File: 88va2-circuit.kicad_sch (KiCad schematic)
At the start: 0 parts

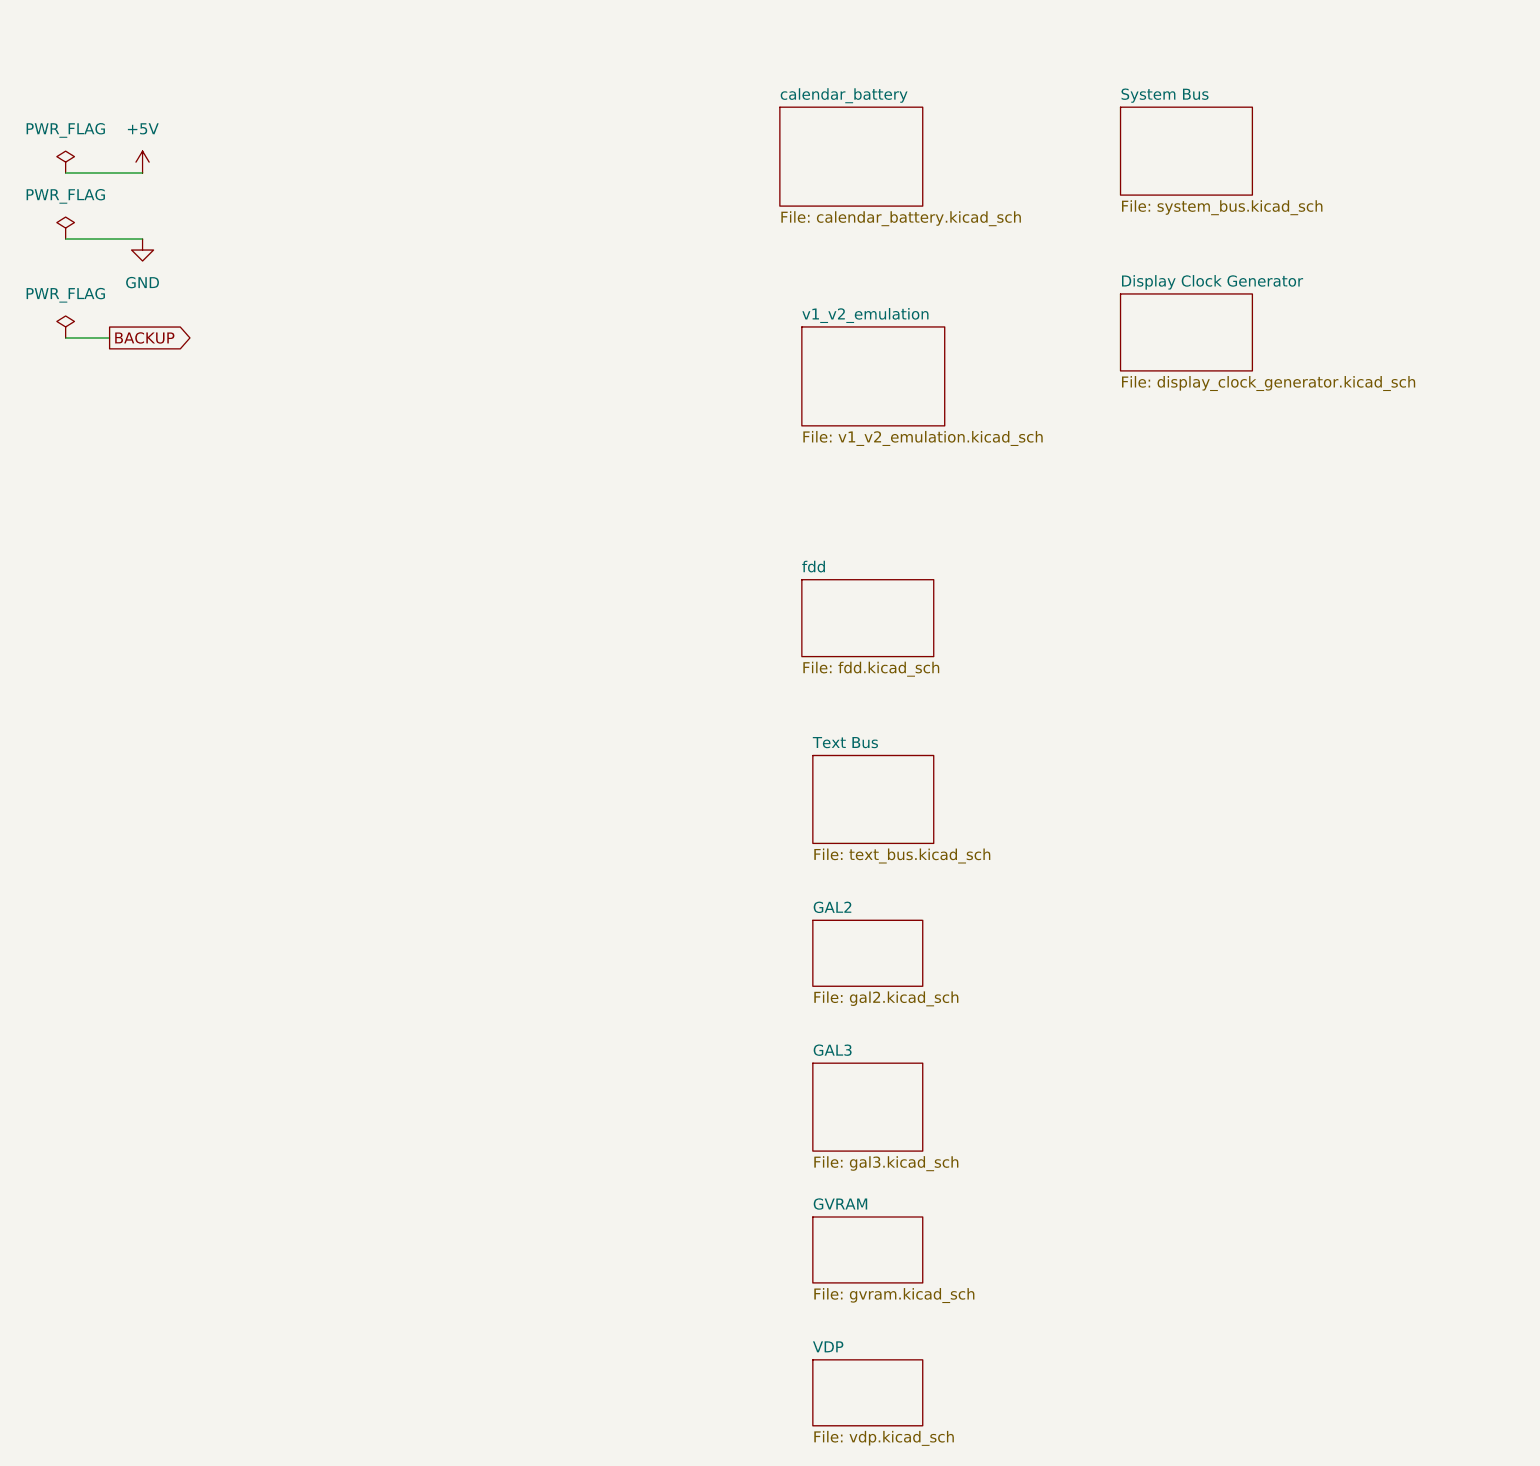
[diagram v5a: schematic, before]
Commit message: schematic: tidy hierarchical sheets
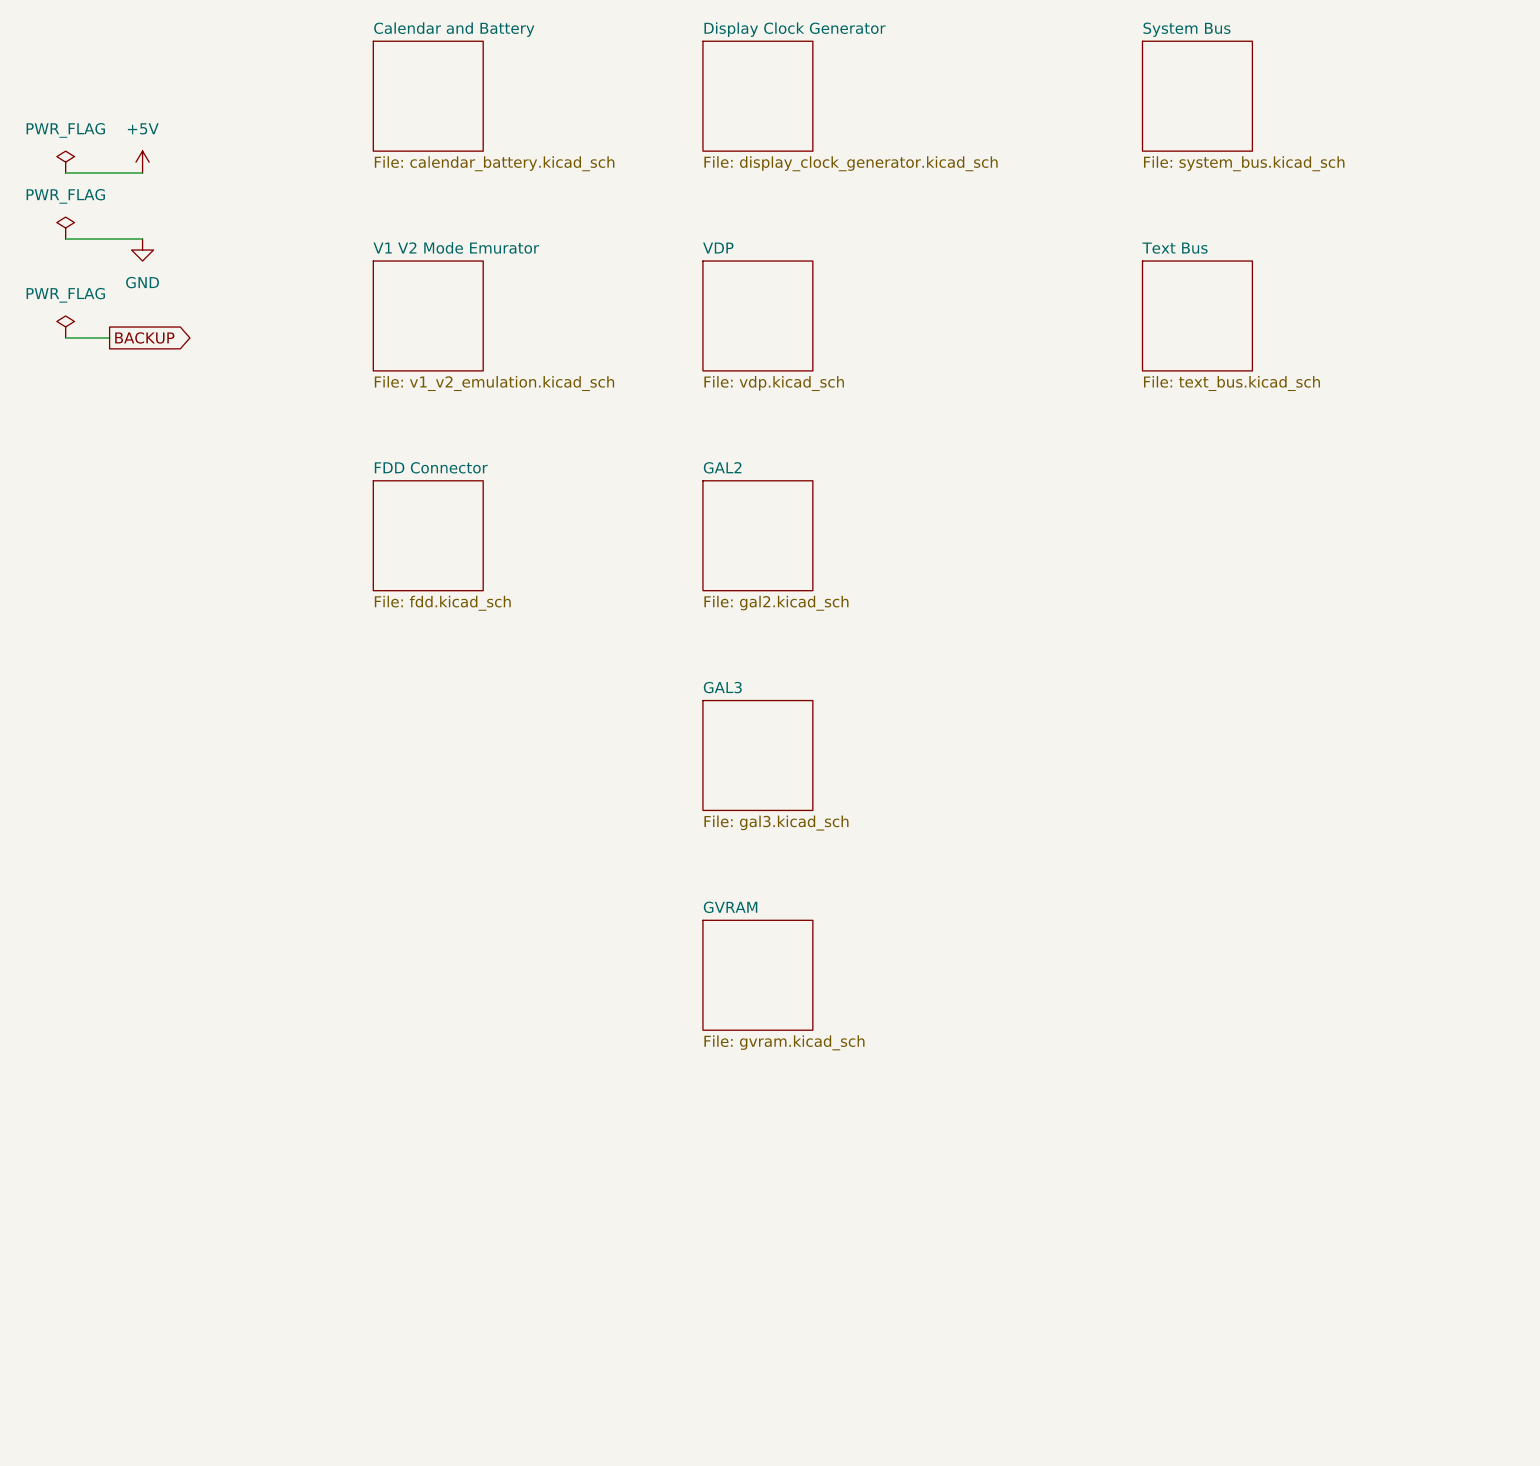
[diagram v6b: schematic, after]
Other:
- sheet calendar_battery renamed Calendar and Battery
- sheet fdd renamed FDD Connector
- sheet v1_v2_emulation renamed V1 V2 Mode Emurator
- title: (none) -> PC-88VA2 メイン基板 PWD-665
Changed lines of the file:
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@@
 (kicad_sch (version 20230121) (generator eeschema)
   (paper "A4")
+  (title_block
+    (title "PC-88VA2 メイン基板 PWD-665")
+  )
   (wire (pts (xy 40.64 59.69) (xy 45.72 59.69))
     (stroke (width 0) (type default))
@@
     )
   )
-  (sheet (at 125.73 87.63) (size 15.24 8.89) (fields_autoplaced)
-    (stroke (width 0.1524) (type solid))
-    (fill (color 0 0 0 0.0000))
-    (property "Sheetname" "fdd" (at 125.73 86.9184 0)
-      (effects (font (size 1.27 1.27)) (justify left bottom))
-    )
-    (property "Sheetfile" "fdd.kicad_sch" (at 125.73 97.1046 0)
+  (sheet (at 76.2 76.2) (size 12.7 12.7) (fields_autoplaced)
+    (stroke (width 0.1524) (type solid))
+    (fill (color 0 0 0 0.0000))
+    (property "Sheetname" "FDD Connector" (at 76.2 75.4884 0)
+      (effects (font (size 1.27 1.27)) (justify left bottom))
+    )
+    (property "Sheetfile" "fdd.kicad_sch" (at 76.2 89.4846 0)
       (effects (font (size 1.27 1.27)) (justify left top))
     )
@@
     )
   )
-  (sheet (at 125.73 58.42) (size 16.51 11.43) (fields_autoplaced)
-    (stroke (width 0.1524) (type solid))
-    (fill (color 0 0 0 0.0000))
-    (property "Sheetname" "v1_v2_emulation" (at 125.73 57.7084 0)
-      (effects (font (size 1.27 1.27)) (justify left bottom))
-    )
-    (property "Sheetfile" "v1_v2_emulation.kicad_sch" (at 125.73 70.4346 0)
+  (sheet (at 76.2 50.8) (size 12.7 12.7) (fields_autoplaced)
+    (stroke (width 0.1524) (type solid))
+    (fill (color 0 0 0 0.0000))
+    (property "Sheetname" "V1 V2 Mode Emurator" (at 76.2 50.0884 0)
+      (effects (font (size 1.27 1.27)) (justify left bottom))
+    )
+    (property "Sheetfile" "v1_v2_emulation.kicad_sch" (at 76.2 64.0846 0)
       (effects (font (size 1.27 1.27)) (justify left top))
     )
@@
     )
   )
-  (sheet (at 162.56 33.02) (size 15.24 10.16) (fields_autoplaced)
-    (stroke (width 0.1524) (type solid))
-    (fill (color 0 0 0 0.0000))
-    (property "Sheetname" "System Bus" (at 162.56 32.3084 0)
-      (effects (font (size 1.27 1.27)) (justify left bottom))
-    )
-    (property "Sheetfile" "system_bus.kicad_sch" (at 162.56 43.7646 0)
+  (sheet (at 165.1 25.4) (size 12.7 12.7) (fields_autoplaced)
+    (stroke (width 0.1524) (type solid))
+    (fill (color 0 0 0 0.0000))
+    (property "Sheetname" "System Bus" (at 165.1 24.6884 0)
+      (effects (font (size 1.27 1.27)) (justify left bottom))
+    )
+    (property "Sheetfile" "system_bus.kicad_sch" (at 165.1 38.6846 0)
       (effects (font (size 1.27 1.27)) (justify left top))
     )
@@
     )
   )
-  (sheet (at 127 143.51) (size 12.7 10.16) (fields_autoplaced)
-    (stroke (width 0.1524) (type solid))
-    (fill (color 0 0 0 0.0000))
-    (property "Sheetname" "GAL3" (at 127 142.7984 0)
-      (effects (font (size 1.27 1.27)) (justify left bottom))
-    )
-    (property "Sheetfile" "gal3.kicad_sch" (at 127 154.2546 0)
+  (sheet (at 114.3 101.6) (size 12.7 12.7) (fields_autoplaced)
+    (stroke (width 0.1524) (type solid))
+    (fill (color 0 0 0 0.0000))
+    (property "Sheetname" "GAL3" (at 114.3 100.8884 0)
+      (effects (font (size 1.27 1.27)) (justify left bottom))
+    )
+    (property "Sheetfile" "gal3.kicad_sch" (at 114.3 114.8846 0)
       (effects (font (size 1.27 1.27)) (justify left top))
     )
@@
     )
   )
-  (sheet (at 127 161.29) (size 12.7 7.62) (fields_autoplaced)
-    (stroke (width 0.1524) (type solid))
-    (fill (color 0 0 0 0.0000))
-    (property "Sheetname" "GVRAM" (at 127 160.5784 0)
-      (effects (font (size 1.27 1.27)) (justify left bottom))
-    )
-    (property "Sheetfile" "gvram.kicad_sch" (at 127 169.4946 0)
+  (sheet (at 114.3 127) (size 12.7 12.7) (fields_autoplaced)
+    (stroke (width 0.1524) (type solid))
+    (fill (color 0 0 0 0.0000))
+    (property "Sheetname" "GVRAM" (at 114.3 126.2884 0)
+      (effects (font (size 1.27 1.27)) (justify left bottom))
+    )
+    (property "Sheetfile" "gvram.kicad_sch" (at 114.3 140.2846 0)
       (effects (font (size 1.27 1.27)) (justify left top))
     )
@@
     )
   )
-  (sheet (at 127 107.95) (size 13.97 10.16) (fields_autoplaced)
-    (stroke (width 0.1524) (type solid))
-    (fill (color 0 0 0 0.0000))
-    (property "Sheetname" "Text Bus" (at 127 107.2384 0)
-      (effects (font (size 1.27 1.27)) (justify left bottom))
-    )
-    (property "Sheetfile" "text_bus.kicad_sch" (at 127 118.6946 0)
+  (sheet (at 165.1 50.8) (size 12.7 12.7) (fields_autoplaced)
+    (stroke (width 0.1524) (type solid))
+    (fill (color 0 0 0 0.0000))
+    (property "Sheetname" "Text Bus" (at 165.1 50.0884 0)
+      (effects (font (size 1.27 1.27)) (justify left bottom))
+    )
+    (property "Sheetfile" "text_bus.kicad_sch" (at 165.1 64.0846 0)
       (effects (font (size 1.27 1.27)) (justify left top))
     )
@@
     )
   )
-  (sheet (at 162.56 54.61) (size 15.24 8.89) (fields_autoplaced)
-    (stroke (width 0.1524) (type solid))
-    (fill (color 0 0 0 0.0000))
-    (property "Sheetname" "Display Clock Generator" (at 162.56 53.8984 0)
-      (effects (font (size 1.27 1.27)) (justify left bottom))
-    )
-    (property "Sheetfile" "display_clock_generator.kicad_sch" (at 162.56 64.0846 0)
+  (sheet (at 114.3 25.4) (size 12.7 12.7) (fields_autoplaced)
+    (stroke (width 0.1524) (type solid))
+    (fill (color 0 0 0 0.0000))
+    (property "Sheetname" "Display Clock Generator" (at 114.3 24.6884 0)
+      (effects (font (size 1.27 1.27)) (justify left bottom))
+    )
+    (property "Sheetfile" "display_clock_generator.kicad_sch" (at 114.3 38.6846 0)
       (effects (font (size 1.27 1.27)) (justify left top))
     )
@@
     )
   )
-  (sheet (at 127 177.8) (size 12.7 7.62) (fields_autoplaced)
-    (stroke (width 0.1524) (type solid))
-    (fill (color 0 0 0 0.0000))
-    (property "Sheetname" "VDP" (at 127 177.0884 0)
-      (effects (font (size 1.27 1.27)) (justify left bottom))
-    )
-    (property "Sheetfile" "vdp.kicad_sch" (at 127 186.0046 0)
+  (sheet (at 114.3 50.8) (size 12.7 12.7) (fields_autoplaced)
+    (stroke (width 0.1524) (type solid))
+    (fill (color 0 0 0 0.0000))
+    (property "Sheetname" "VDP" (at 114.3 50.0884 0)
+      (effects (font (size 1.27 1.27)) (justify left bottom))
+    )
+    (property "Sheetfile" "vdp.kicad_sch" (at 114.3 64.0846 0)
       (effects (font (size 1.27 1.27)) (justify left top))
     )
@@
     )
   )
-  (sheet (at 123.19 33.02) (size 16.51 11.43) (fields_autoplaced)
-    (stroke (width 0.1524) (type solid))
-    (fill (color 0 0 0 0.0000))
-    (property "Sheetname" "calendar_battery" (at 123.19 32.3084 0)
-      (effects (font (size 1.27 1.27)) (justify left bottom))
-    )
-    (property "Sheetfile" "calendar_battery.kicad_sch" (at 123.19 45.0346 0)
+  (sheet (at 76.2 25.4) (size 12.7 12.7) (fields_autoplaced)
+    (stroke (width 0.1524) (type solid))
+    (fill (color 0 0 0 0.0000))
+    (property "Sheetname" "Calendar and Battery" (at 76.2 24.6884 0)
+      (effects (font (size 1.27 1.27)) (justify left bottom))
+    )
+    (property "Sheetfile" "calendar_battery.kicad_sch" (at 76.2 38.6846 0)
       (effects (font (size 1.27 1.27)) (justify left top))
     )
@@
     )
   )
-  (sheet (at 127 127) (size 12.7 7.62) (fields_autoplaced)
-    (stroke (width 0.1524) (type solid))
-    (fill (color 0 0 0 0.0000))
-    (property "Sheetname" "GAL2" (at 127 126.2884 0)
-      (effects (font (size 1.27 1.27)) (justify left bottom))
-    )
-    (property "Sheetfile" "gal2.kicad_sch" (at 127 135.2046 0)
-      (effects (font (size 1.27 1.27)) (justify left top))
-    )
+  (sheet (at 114.3 76.2) (size 12.7 12.7) (fields_autoplaced)
+    (stroke (width 0.1524) (type solid))
+    (fill (color 0 0 0 0.0000))
+    (property "Sheetname" "GAL2" (at 114.3 75.4884 0)
+      (effects (font (size 1.27 1.27)) (justify left bottom))
+    )
+    (property "Sheetfile" "gal2.kicad_sch" (at 114.3 89.4846 0)
+      (effects (font (size 1.27 1.27)) (justify left top))
+    )
